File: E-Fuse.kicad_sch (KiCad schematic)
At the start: 4 parts, among them U4 TPS16630PWPR

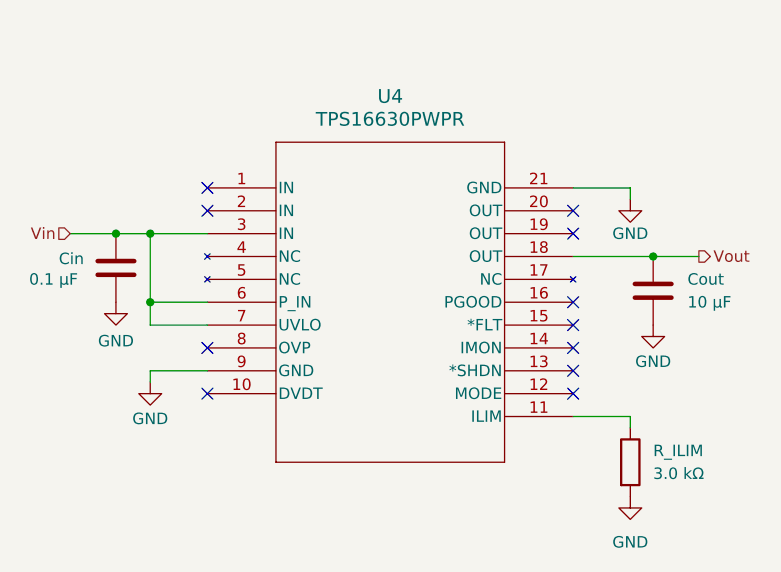
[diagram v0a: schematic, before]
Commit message: added footprints
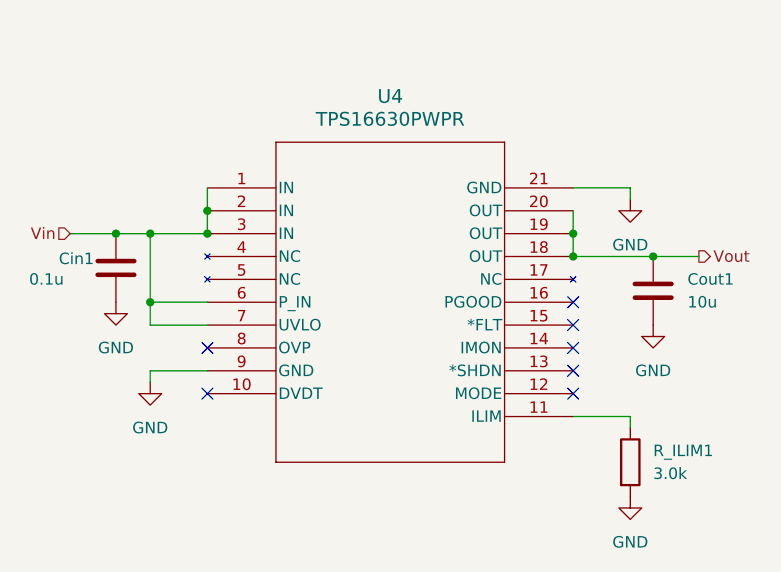
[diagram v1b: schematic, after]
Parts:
- Cin1: renamed from Cin; value 0.1 µF -> 0.1u; footprint (none) -> Capacitor_SMD:C_0805_2012Metric
- Cout1: renamed from Cout; value 10 µF -> 10u; footprint (none) -> Capacitor_SMD:C_0805_2012Metric
- R_ILIM1: renamed from R_ILIM; value 3.0 kΩ -> 3.0k; footprint (none) -> Resistor_SMD:R_0805_2012Metric
- U4: footprint HTSSOP20_PWP_TEX -> (none)
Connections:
- net Vin: now also U4.1 (IN), U4.2 (IN)
- net Vout: now also U4.19 (OUT), U4.20 (OUT)
- no-connect marks 11 -> 7

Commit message: testing
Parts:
- Cin: renamed from Cin1; value 0.1u -> 0.1 µF; footprint Capacitor_SMD:C_0805_2012Metric -> (none)
- Cout: renamed from Cout1; value 10u -> 10 µF; footprint Capacitor_SMD:C_0805_2012Metric -> (none)
- R_ILIM: renamed from R_ILIM1; value 3.0k -> 3.0 kΩ; footprint Resistor_SMD:R_0805_2012Metric -> (none)
- U4: footprint (none) -> HTSSOP20_PWP_TEX
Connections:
- net Vin: no longer U4.1 (IN), U4.2 (IN)
- net Vout: no longer U4.19 (OUT), U4.20 (OUT)
- no-connect marks 7 -> 11
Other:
- note added: "E-Fuse"

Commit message: capacitor
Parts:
- Cin: value 0.1 µF -> 0.1u; Digikey (none) -> 1276-1003-1-ND; LCSC (none) -> C1711; MPN (none) -> CL21B104KBCNNNC; Manufacturer (none) -> Samsung Electro-Mechanics
- Cout: value 10 µF -> 10u; Digikey (none) -> 1276-6698-1-ND; MPN (none) -> CL21X106KAYNNNE; Manufacturer (none) -> Samsung Electro-Mechanics
- R_ILIM: value 3.0 kΩ -> 3.0k
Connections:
- net Vin: now also U4.1 (IN), U4.2 (IN)
- net Vout: now also U4.19 (OUT), U4.20 (OUT)
- no-connect marks 11 -> 7
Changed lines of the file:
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@@
+	)
+	(junction
+		(at 163.83 91.44)
+		(diameter 0)
+		(color 0 0 0 0)
+	)
+	(junction
+		(at 163.83 88.9)
+		(diameter 0)
+		(color 0 0 0 0)
 	)
 	(junction
@@
 	)
 	(junction
+		(at 116.84 86.36)
+		(diameter 0)
+		(color 0 0 0 0)
+	)
+	(junction
 		(at 116.84 96.52)
 		(diameter 0)
@@
 	)
 	(no_connect
-		(at 123.19 83.82)
-	)
-	(no_connect
 		(at 163.83 106.68)
-	)
-	(no_connect
-		(at 163.83 88.9)
 	)
 	(no_connect
@@
 	)
 	(no_connect
-		(at 163.83 86.36)
-	)
-	(no_connect
-		(at 123.19 86.36)
-	)
-	(no_connect
 		(at 163.83 101.6)
 	)
@@
 	(wire
 		(pts
+			(xy 116.84 86.36) (xy 116.84 88.9)
+		)
+		(stroke
+			(width 0)
+			(type default)
+		)
+	)
+	(wire
+		(pts
 			(xy 116.84 96.52) (xy 123.19 96.52)
 		)
@@
 	(wire
 		(pts
+			(xy 116.84 83.82) (xy 116.84 86.36)
+		)
+		(stroke
+			(width 0)
+			(type default)
+		)
+	)
+	(wire
+		(pts
 			(xy 123.19 104.14) (xy 116.84 104.14)
 		)
@@
 	(wire
 		(pts
+			(xy 163.83 88.9) (xy 163.83 91.44)
+		)
+		(stroke
+			(width 0)
+			(type default)
+		)
+	)
+	(wire
+		(pts
 			(xy 170.18 83.82) (xy 170.18 85.09)
 		)
@@
 	(wire
 		(pts
+			(xy 163.83 86.36) (xy 163.83 88.9)
+		)
+		(stroke
+			(width 0)
+			(type default)
+		)
+	)
+	(wire
+		(pts
 			(xy 116.84 96.52) (xy 116.84 88.9)
 		)
@@
 	(wire
 		(pts
+			(xy 116.84 86.36) (xy 123.19 86.36)
+		)
+		(stroke
+			(width 0)
+			(type default)
+		)
+	)
+	(wire
+		(pts
 			(xy 170.18 109.22) (xy 170.18 110.49)
 		)
@@
 		(pts
 			(xy 116.84 99.06) (xy 116.84 96.52)
+		)
+		(stroke
+			(width 0)
+			(type default)
+		)
+	)
+	(wire
+		(pts
+			(xy 116.84 83.82) (xy 123.19 83.82)
 		)
 		(stroke
@@
 			)
 		)
-		(property "Value" "3.0 kΩ"
+		(property "Value" "3.0k"
 			(at 172.72 115.5699 0)
 			(show_name no)
@@
 			)
 		)
-		(property "Value" "10 µF"
+		(property "Value" "10u"
 			(at 176.53 96.5199 0)
 			(show_name no)
@@
 		)
 		(property "Description" "Unpolarized capacitor"
+			(at 172.72 95.25 0)
+			(hide yes)
+			(show_name no)
+			(do_not_autoplace no)
+			(effects
+				(font
+					(size 1.27 1.27)
+				)
+			)
+		)
+		(property "Digikey" "1276-6698-1-ND"
+			(at 172.72 95.25 0)
+			(hide yes)
+			(show_name no)
+			(do_not_autoplace no)
+			(effects
+				(font
+					(size 1.27 1.27)
+				)
+			)
+		)
+		(property "MPN" "CL21X106KAYNNNE"
+			(at 172.72 95.25 0)
+			(hide yes)
+			(show_name no)
+			(do_not_autoplace no)
+			(effects
+				(font
+					(size 1.27 1.27)
+				)
+			)
+		)
+		(property "Manufacturer" "Samsung Electro-Mechanics"
 			(at 172.72 95.25 0)
 			(hide yes)
@@
 			)
 		)
-		(property "Value" "0.1 µF"
-			(at 103.378 93.98 0)
+		(property "Value" "0.1u"
+			(at 105.918 93.726 0)
 			(show_name no)
 			(do_not_autoplace no)
@@
 			(at 113.03 92.71 0)
 			(hide yes)
+			(show_name no)
+			(do_not_autoplace no)
+			(effects
+				(font
+					(size 1.27 1.27)
+				)
+			)
+		)
+		(property "Digikey" "1276-1003-1-ND"
+			(at 113.03 92.71 0)
+			(hide yes)
+			(show_name no)
+			(do_not_autoplace no)
+			(effects
+				(font
+					(size 1.27 1.27)
+				)
+			)
+		)
+		(property "LCSC" "C1711"
+			(at 113.03 92.71 0)
+			(hide yes)
+			(show_name no)
+			(do_not_autoplace no)
+			(effects
+				(font
+					(size 1.27 1.27)
+				)
+			)
+		)
+		(property "MPN" "CL21B104KBCNNNC"
+			(at 113.03 92.71 0)
+			(hide yes)
+			(show_name no)
+			(do_not_autoplace no)
+			(effects
+				(font
+					(size 1.27 1.27)
+				)
+			)
+		)
+		(property "Manufacturer" "Samsung Electro-Mechanics"
+			(at 113.03 92.71 0)
+			(hide yes)
